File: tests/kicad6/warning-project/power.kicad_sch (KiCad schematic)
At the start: 2 parts, among them P1 CONN_01X02

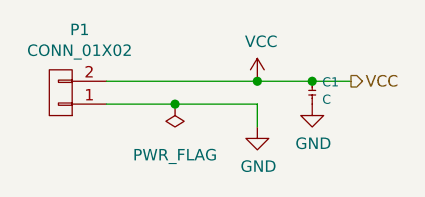
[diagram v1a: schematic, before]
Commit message: Fixed KiCad 6 warning example.
Missing PWR_FLG, now detected by nightly.
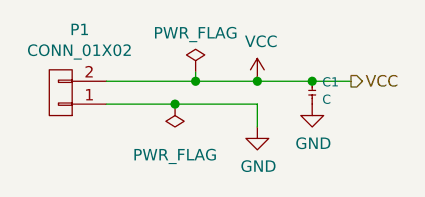
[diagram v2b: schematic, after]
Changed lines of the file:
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@@
-(kicad_sch (version 20200828) (generator eeschema)
-  (page 2 3)
+(kicad_sch (version 20201015) (generator eeschema)
+  (page 1 3)
   (paper "A4")
   (junction (at 123.19 92.964) (diameter 1.016) (color 0 0 0 0))
+  (junction (at 125.476 90.424) (diameter 1.016) (color 0 0 0 0))
   (junction (at 132.334 90.424) (diameter 1.016) (color 0 0 0 0))
   (junction (at 138.43 90.424) (diameter 1.016) (color 0 0 0 0))
-  (wire (pts (xy 115.57 90.424) (xy 132.334 90.424))
+  (wire (pts (xy 115.57 90.424) (xy 125.476 90.424))
     (stroke (width 0) (type solid) (color 0 0 0 0))
   )
@@
   )
   (wire (pts (xy 123.19 92.964) (xy 132.334 92.964))
+    (stroke (width 0) (type solid) (color 0 0 0 0))
+  )
+  (wire (pts (xy 125.476 89.408) (xy 125.476 90.424))
+    (stroke (width 0) (type solid) (color 0 0 0 0))
+  )
+  (wire (pts (xy 125.476 90.424) (xy 132.334 90.424))
     (stroke (width 0) (type solid) (color 0 0 0 0))
   )
@@
     (property "Datasheet" "" (id 3) (at 123.19 92.964 0))
   )
+  (symbol (lib_id "power:PWR_FLAG") (at 125.476 89.408 0) (unit 1)
+    (in_bom yes) (on_board yes)
+    (property "Reference" "#FLG0101" (id 0) (at 125.476 87.503 0)
+      (effects (font (size 1.27 1.27)) hide)
+    )
+    (property "Value" "PWR_FLAG" (id 1) (at 125.476 85.0836 0))
+    (property "Footprint" "" (id 2) (at 125.476 89.408 0)
+      (effects (font (size 1.27 1.27)) hide)
+    )
+    (property "Datasheet" "~" (id 3) (at 125.476 89.408 0)
+      (effects (font (size 1.27 1.27)) hide)
+    )
+  )
   (symbol (lib_id "power:VCC") (at 132.334 90.424 0) (unit 1)
